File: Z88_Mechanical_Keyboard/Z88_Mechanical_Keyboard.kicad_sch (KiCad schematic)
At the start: 66 parts, among them SW1 SHIFT_RH, SW10 SHIFT_LH, SW11 SPACE, SW12 LEFT, SW13 RIGHT, SW14 DOWN, SW15 UP, SW16 ENTER, SW17 ESC, SW18 TAB, SW19 1, SW2 HELP, SW20 2, SW21 3, SW22 4, SW23 5, SW24 6, SW25 INDEX, SW26 DIAMOND, SW27 Q, SW28 W, SW29 E, SW3 [, SW30 R, SW31 T, SW32 Y, SW33 CAPS_LOCK, SW34 MENU, SW35 A, SW36 S, SW37 D, SW38 F, SW39 G, SW4 ], SW40 H, SW41 DOT, SW42 COMMA, SW43 Z, SW44 X, SW45 C, SW46 V, SW47 B, SW48 N, SW49 /, SW5 UNDERSCORE, SW50 SEMICOLON, SW51 L, SW52 M, SW53 K, SW54 J, SW55 U, SW56 7, SW57 £, SW58 DOUBLE_QUOTE, SW59 0, SW6 =, SW60 P, SW61 9, SW62 O, SW63 I, SW64 8, SW7 \, SW8 DELETE, SW9 SQUARE

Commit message: Progress commit
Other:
- company: (none) -> Brett Hallen
- title: (none) -> Z88 Mechanical Keyboard
- moved on the sheet: SK7
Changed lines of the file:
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@@
 	(generator_version "9.0")
 	(paper "A4")
+	(title_block
+		(title "Z88 Mechanical Keyboard")
+		(date "1-Jul-2025")
+		(rev "WIP")
+		(company "Brett Hallen")
+		(comment 1 "www.youtube.com/@Brfff")
+	)
 	(text_box "Columns      Rows\nCOL0 = A15   ROW0 = D7\nCOL1 = A14   ROW1 = D6\nCOL2 = A13   ROW2 = D5\nCOL3 = A12   ROW3 = D4\nCOL4 = A11   ROW4 = D3\nCOL5 = A10   ROW5 = D2\nCOL6 = A9    ROW6 = D1\nCOL7 = A8    ROW7 = D0"
 		(exclude_from_sim no)
@@
 	(global_label "ROW5"
 		(shape input)
-		(at 254 46.99 180)
+		(at 256.54 39.37 270)
 		(fields_autoplaced yes)
 		(effects
@@
 		)
 		(property "Intersheetrefs" "${INTERSHEET_REFS}"
-			(at 245.7534 46.99 0)
+			(at 256.54 47.6166 90)
 			(effects
 				(font
@@
 	(global_label "ROW2"
 		(shape input)
-		(at 254 29.21 180)
+		(at 238.76 39.37 270)
 		(fields_autoplaced yes)
 		(effects
@@
 		)
 		(property "Intersheetrefs" "${INTERSHEET_REFS}"
-			(at 245.7534 29.21 0)
+			(at 238.76 47.6166 90)
 			(effects
 				(font
@@
 	(global_label "ROW6"
 		(shape input)
-		(at 254 36.83 180)
+		(at 246.38 39.37 270)
 		(fields_autoplaced yes)
 		(effects
@@
 		)
 		(property "Intersheetrefs" "${INTERSHEET_REFS}"
-			(at 245.7534 36.83 0)
+			(at 246.38 47.6166 90)
 			(effects
 				(font
@@
 	(global_label "ROW4"
 		(shape input)
-		(at 254 34.29 180)
+		(at 243.84 39.37 270)
 		(fields_autoplaced yes)
 		(effects
@@
 		)
 		(property "Intersheetrefs" "${INTERSHEET_REFS}"
-			(at 245.7534 34.29 0)
+			(at 243.84 47.6166 90)
 			(effects
 				(font
@@
 	(global_label "ROW0"
 		(shape input)
-		(at 254 39.37 180)
+		(at 248.92 39.37 270)
 		(fields_autoplaced yes)
 		(effects
@@
 		)
 		(property "Intersheetrefs" "${INTERSHEET_REFS}"
-			(at 245.7534 39.37 0)
+			(at 248.92 47.6166 90)
 			(effects
 				(font
@@
 	(global_label "ROW7"
 		(shape input)
-		(at 254 41.91 180)
+		(at 251.46 39.37 270)
 		(fields_autoplaced yes)
 		(effects
@@
 		)
 		(property "Intersheetrefs" "${INTERSHEET_REFS}"
-			(at 245.7534 41.91 0)
+			(at 251.46 47.6166 90)
 			(effects
 				(font
@@
 	(global_label "ROW3"
 		(shape input)
-		(at 254 31.75 180)
+		(at 241.3 39.37 270)
 		(fields_autoplaced yes)
 		(effects
@@
 		)
 		(property "Intersheetrefs" "${INTERSHEET_REFS}"
-			(at 245.7534 31.75 0)
+			(at 241.3 47.6166 90)
 			(effects
 				(font
@@
 	(global_label "ROW1"
 		(shape input)
-		(at 254 44.45 180)
+		(at 254 39.37 270)
 		(fields_autoplaced yes)
 		(effects
@@
 		)
 		(property "Intersheetrefs" "${INTERSHEET_REFS}"
-			(at 245.7534 44.45 0)
+			(at 254 47.6166 90)
 			(effects
 				(font
@@
 	(symbol
 		(lib_id "Connector_Generic:Conn_01x08")
-		(at 259.08 36.83 0)
+		(at 246.38 34.29 90)
 		(unit 1)
 		(exclude_from_sim no)
@@
 		(on_board yes)
 		(dnp no)
-		(fields_autoplaced yes)
 		(property "Reference" "SK7"
-			(at 261.62 36.8299 0)
+			(at 248.92 27.94 90)
 			(effects
 				(font
@@
 		)
 		(property "Value" "Z80 Data Bus"
-			(at 261.62 39.3699 0)
+			(at 251.46 30.48 90)
 			(effects
 				(font
@@
 		)
 		(property "Footprint" "Connector_PinHeader_2.54mm:PinHeader_1x08_P2.54mm_Horizontal"
-			(at 259.08 36.83 0)
+			(at 246.38 34.29 0)
 			(effects
 				(font
@@
 		)
 		(property "Datasheet" "~"
-			(at 259.08 36.83 0)
+			(at 246.38 34.29 0)
 			(effects
 				(font
@@
 		)
 		(property "Description" "Generic connector, single row, 01x08, script generated (kicad-library-utils/schlib/autogen/connector/)"
-			(at 259.08 36.83 0)
+			(at 246.38 34.29 0)
 			(effects
 				(font

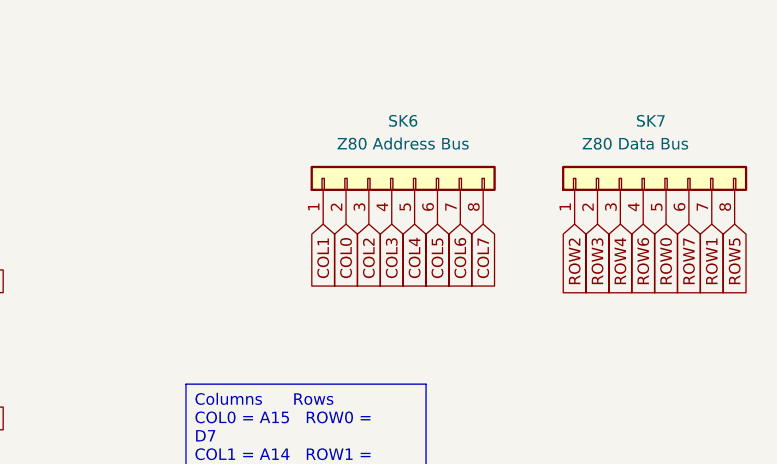
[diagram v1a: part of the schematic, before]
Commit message: Added 3D models
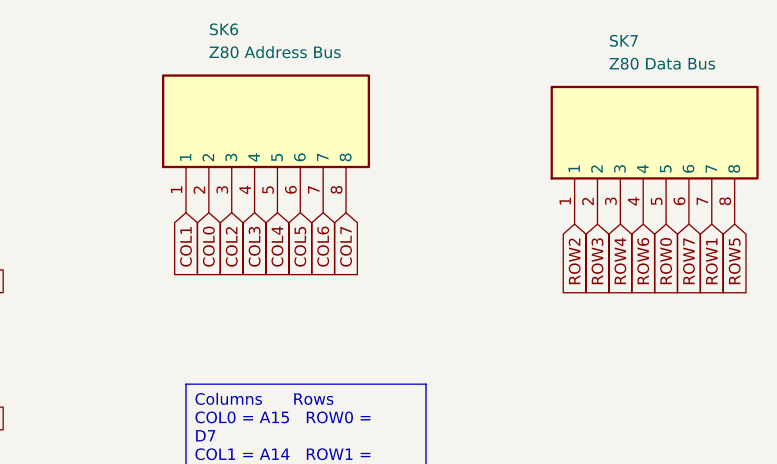
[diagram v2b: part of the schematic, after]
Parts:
- removed SK6: Z80 Address Bus, Connector_PinHeader_2.54mm:PinHeader_1x08_P2.54mm_Horizontal, symbol Connector_Generic:Conn_01x08
- removed SK7: Z80 Data Bus, Connector_PinHeader_2.54mm:PinHeader_1x08_P2.54mm_Horizontal, symbol Connector_Generic:Conn_01x08
- added SK6: Z80 Address Bus, Clueless_Engineer:55203148, symbol Clueless_Engineer:5-520314-8
- added SK7: Z80 Data Bus, Clueless_Engineer:55203148, symbol Clueless_Engineer:5-520314-8
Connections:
- net COL0: now also SK6.2
- net COL1: now also SK6.1
- net COL2: now also SK6.3
- net COL3: now also SK6.4
- net COL4: now also SK6.5
- net COL5: now also SK6.6
- net COL6: now also SK6.7
- net COL7: now also SK6.8
- net ROW0: now also SK7.5
- net ROW1: now also SK7.7
- net ROW2: now also SK7.1
- net ROW3: now also SK7.2
- net ROW4: now also SK7.3
- net ROW5: now also SK7.8
- net ROW6: now also SK7.4
- net ROW7: now also SK7.6

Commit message: Keyboard layout changes
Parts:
- added H1, H2: MountingHole, MountingHole:MountingHole_3.2mm_M3, symbol Mechanical:MountingHole
- SW19: value 1 -> ONE
- SW49: value / -> /FORWSLASH/
- SW57: value £ -> GBP
- SW59: value 0 -> ZERO
- SW6: value = -> EQUALS
- SW7: value \ -> \BACKSLASH\
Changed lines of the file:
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@@
 	)
 	(symbol
+		(lib_id "Mechanical:MountingHole")
+		(at 205.74 106.68 0)
+		(unit 1)
+		(exclude_from_sim yes)
+		(in_bom no)
+		(on_board yes)
+		(dnp no)
+		(fields_autoplaced yes)
+		(property "Reference" "H1"
+			(at 208.28 105.4099 0)
+			(effects
+				(font
+					(size 1.27 1.27)
+				)
+				(justify left)
+			)
+		)
+		(property "Value" "MountingHole"
+			(at 208.28 107.9499 0)
+			(effects
+				(font
+					(size 1.27 1.27)
+				)
+				(justify left)
+			)
+		)
+		(property "Footprint" "MountingHole:MountingHole_3.2mm_M3"
+			(at 205.74 106.68 0)
+			(effects
+				(font
+					(size 1.27 1.27)
+				)
+				(hide yes)
+			)
+		)
+		(property "Datasheet" "~"
+			(at 205.74 106.68 0)
+			(effects
+				(font
+					(size 1.27 1.27)
+				)
+				(hide yes)
+			)
+		)
+		(property "Description" "Mounting Hole without connection"
+			(at 205.74 106.68 0)
+			(effects
+				(font
+					(size 1.27 1.27)
+				)
+				(hide yes)
+			)
+		)
+		(instances
+			(project ""
+				(path "/52bc2244-0402-458b-a824-605619f8f036"
+					(reference "H1")
+					(unit 1)
+				)
+			)
+		)
+	)
+	(symbol
 		(lib_id "Switch:SW_Push_45deg")
 		(at 165.1 43.18 0)
@@
 			)
 		)
-		(property "Value" "1"
+		(property "Value" "ONE"
 			(at 82.55 69.85 0)
 			(effects
@@
 			)
 		)
-		(property "Value" "/"
+		(property "Value" "/FORWSLASH/"
 			(at 49.53 132.08 0)
 			(effects
@@
 			)
 		)
-		(property "Value" "="
+		(property "Value" "EQUALS"
 			(at 132.08 38.1 0)
 			(effects
@@
 			)
 		)
-		(property "Value" "\\"
+		(property "Value" "\\BACKSLASH\\"
 			(at 148.59 38.1 0)
 			(effects
@@
 			)
 		)
-		(property "Value" "0"
+		(property "Value" "ZERO"
 			(at 82.55 147.32 0)
 			(effects
@@
 	)
 	(symbol
+		(lib_id "Mechanical:MountingHole")
+		(at 205.74 114.3 0)
+		(unit 1)
+		(exclude_from_sim yes)
+		(in_bom no)
+		(on_board yes)
+		(dnp no)
+		(fields_autoplaced yes)
+		(property "Reference" "H2"
+			(at 208.28 113.0299 0)
+			(effects
+				(font
+					(size 1.27 1.27)
+				)
+				(justify left)
+			)
+		)
+		(property "Value" "MountingHole"
+			(at 208.28 115.5699 0)
+			(effects
+				(font
+					(size 1.27 1.27)
+				)
+				(justify left)
+			)
+		)
+		(property "Footprint" "MountingHole:MountingHole_3.2mm_M3"
+			(at 205.74 114.3 0)
+			(effects
+				(font
+					(size 1.27 1.27)
+				)
+				(hide yes)
+			)
+		)
+		(property "Datasheet" "~"
+			(at 205.74 114.3 0)
+			(effects
+				(font
+					(size 1.27 1.27)
+				)
+				(hide yes)
+			)
+		)
+		(property "Description" "Mounting Hole without connection"
+			(at 205.74 114.3 0)
+			(effects
+				(font
+					(size 1.27 1.27)
+				)
+				(hide yes)
+			)
+		)
+		(instances
+			(project "Z88_Mechanical_Keyboard"
+				(path "/52bc2244-0402-458b-a824-605619f8f036"
+					(reference "H2")
+					(unit 1)
+				)
+			)
+		)
+	)
+	(symbol
 		(lib_id "Switch:SW_Push_45deg")
 		(at 49.53 43.18 0)
@@
 			)
 		)
-		(property "Value" "£"
+		(property "Value" "GBP"
 			(at 49.53 147.32 0)
 			(effects

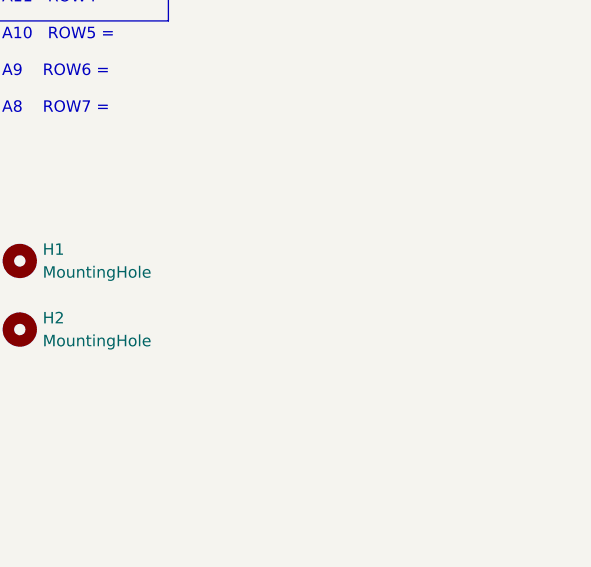
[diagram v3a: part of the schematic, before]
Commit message: Added T-cursor layout
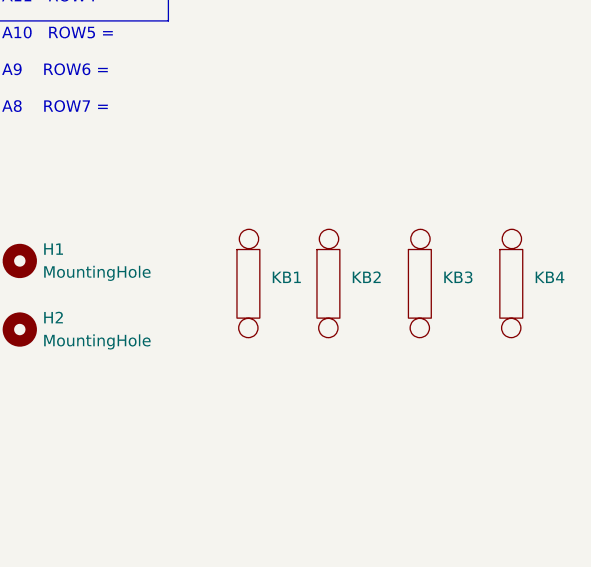
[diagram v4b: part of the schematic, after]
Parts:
- added KB1, KB2, KB3: ~, PCM_Mounting_Keyboard_Stabilizer:Stabilizer_Cherry_MX_2.00u, symbol Clueless_Engineer:Stabiliser
- added KB4: ~, PCM_Mounting_Keyboard_Stabilizer:Stabilizer_Cherry_MX_7.00u, symbol Clueless_Engineer:Stabiliser

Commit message: Routing completed
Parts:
- KB1: value ~ -> SHIFT_LH
- KB2: value ~ -> SHIFT_RH
- KB3: value ~ -> ENTER
- KB4: value ~ -> SPACE_BAR
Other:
- moved on the sheet: KB1, KB2, KB3, KB4
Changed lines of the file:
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@@
 	(title_block
 		(title "Z88 Mechanical Keyboard")
-		(date "1-Jul-2025")
-		(rev "WIP")
+		(date "4-Jul-2025")
+		(rev "A")
 		(company "Brett Hallen")
 		(comment 1 "www.youtube.com/@Brfff")
@@
 	(symbol
 		(lib_id "Clueless_Engineer:Stabiliser")
-		(at 232.41 107.95 0)
+		(at 207.01 127 0)
 		(unit 1)
 		(exclude_from_sim no)
@@
 		(fields_autoplaced yes)
 		(property "Reference" "KB1"
-			(at 233.68 108.5493 0)
+			(at 208.28 127.5993 0)
 			(effects
 				(font
@@
 			)
 		)
-		(property "Value" "~"
-			(at 233.68 110.4544 0)
+		(property "Value" "SHIFT_LH"
+			(at 208.28 129.5044 0)
 			(effects
 				(font
@@
 		)
 		(property "Footprint" "PCM_Mounting_Keyboard_Stabilizer:Stabilizer_Cherry_MX_2.00u"
-			(at 232.41 107.95 0)
+			(at 207.01 127 0)
 			(effects
 				(font
@@
 		)
 		(property "Datasheet" ""
-			(at 232.41 107.95 0)
+			(at 207.01 127 0)
 			(effects
 				(font
@@
 		)
 		(property "Description" ""
-			(at 232.41 107.95 0)
+			(at 207.01 127 0)
 			(effects
 				(font
@@
 	(symbol
 		(lib_id "Clueless_Engineer:Stabiliser")
-		(at 261.62 107.95 0)
+		(at 229.87 134.62 0)
 		(unit 1)
 		(exclude_from_sim no)
@@
 		(fields_autoplaced yes)
 		(property "Reference" "KB4"
-			(at 262.89 108.5493 0)
+			(at 231.14 135.2193 0)
 			(effects
 				(font
@@
 			)
 		)
-		(property "Value" "~"
-			(at 262.89 110.4544 0)
+		(property "Value" "SPACE_BAR"
+			(at 231.14 137.1244 0)
 			(effects
 				(font
@@
 		)
 		(property "Footprint" "PCM_Mounting_Keyboard_Stabilizer:Stabilizer_Cherry_MX_7.00u"
-			(at 261.62 107.95 0)
+			(at 229.87 134.62 0)
 			(effects
 				(font
@@
 		)
 		(property "Datasheet" ""
-			(at 261.62 107.95 0)
+			(at 229.87 134.62 0)
 			(effects
 				(font
@@
 		)
 		(property "Description" ""
-			(at 261.62 107.95 0)
+			(at 229.87 134.62 0)
 			(effects
 				(font
@@
 	(symbol
 		(lib_id "Clueless_Engineer:Stabiliser")
-		(at 241.3 107.95 0)
+		(at 255.27 127 0)
 		(unit 1)
 		(exclude_from_sim no)
@@
 		(fields_autoplaced yes)
 		(property "Reference" "KB2"
-			(at 242.57 108.5493 0)
+			(at 256.54 127.5993 0)
 			(effects
 				(font
@@
 			)
 		)
-		(property "Value" "~"
-			(at 242.57 110.4544 0)
+		(property "Value" "SHIFT_RH"
+			(at 256.54 129.5044 0)
 			(effects
 				(font
@@
 		)
 		(property "Footprint" "PCM_Mounting_Keyboard_Stabilizer:Stabilizer_Cherry_MX_2.00u"
-			(at 241.3 107.95 0)
+			(at 255.27 127 0)
 			(effects
 				(font
@@
 		)
 		(property "Datasheet" ""
-			(at 241.3 107.95 0)
+			(at 255.27 127 0)
 			(effects
 				(font
@@
 		)
 		(property "Description" ""
-			(at 241.3 107.95 0)
+			(at 255.27 127 0)
 			(effects
 				(font
@@
 	(symbol
 		(lib_id "Clueless_Engineer:Stabiliser")
-		(at 251.46 107.95 0)
+		(at 255.27 111.76 0)
 		(unit 1)
 		(exclude_from_sim no)
@@
 		(fields_autoplaced yes)
 		(property "Reference" "KB3"
-			(at 252.73 108.5493 0)
+			(at 256.54 112.3593 0)
 			(effects
 				(font
@@
 			)
 		)
-		(property "Value" "~"
-			(at 252.73 110.4544 0)
+		(property "Value" "ENTER"
+			(at 256.54 114.2644 0)
 			(effects
 				(font
@@
 		)
 		(property "Footprint" "PCM_Mounting_Keyboard_Stabilizer:Stabilizer_Cherry_MX_2.00u"
-			(at 251.46 107.95 0)
+			(at 255.27 111.76 0)
 			(effects
 				(font
@@
 		)
 		(property "Datasheet" ""
-			(at 251.46 107.95 0)
+			(at 255.27 111.76 0)
 			(effects
 				(font
@@
 		)
 		(property "Description" ""
-			(at 251.46 107.95 0)
+			(at 255.27 111.76 0)
 			(effects
 				(font

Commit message: Final tweaks before test fabrication
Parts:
- SW12: value LEFT -> VASEN
- SW13: value RIGHT -> OIKEIN
- SW14: value DOWN -> ALAS
- SW15: value UP -> YLÖS
- SW19: value ONE -> YKSI
- SW2: value HELP -> APUA!
- SW20: value 2 -> KAKSI
- SW21: value 3 -> KOLME
- SW22: value 4 -> NELJÄ
- SW23: value 5 -> VIISI
- SW24: value 6 -> KUUSI
- SW56: value 7 -> SEITSEMÄN
- SW59: value ZERO -> NOLLA
- SW61: value 9 -> YHDEKSÄN
- SW64: value 8 -> KAHDEKSAN
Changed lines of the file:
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@@
 		(comment 1 "www.youtube.com/@Brfff")
 	)
+	(text_box "SUOMI       ENGLISH\nNOLLA     = ZERO\nYKSI      = ONE\nKAKSI     = TWO\nKOLME     = THREE\nNELJÄ     = FOUR\nVIISI     = FIVE\nKUUSI     = SIX\nSEITSEMÄN = SEVEN\nKAHDEKSAN = EIGHT\nYHDEKSÄN  = NINE\n\nVASEN     = LEFT\nOIKEIN    = RIGHT\nYLÖS      = UP\nALAS      = DOWN\nAPUA!     = HELP!"
+		(exclude_from_sim no)
+		(at 226.06 57.15 0)
+		(size 25.4 39.37)
+		(margins 0.9525 0.9525 0.9525 0.9525)
+		(stroke
+			(width 0)
+			(type solid)
+		)
+		(fill
+			(type none)
+		)
+		(effects
+			(font
+				(face "Consolas")
+				(size 1.27 1.27)
+			)
+			(justify left top)
+		)
+	)
 	(text_box "Columns      Rows\nCOL0 = A15   ROW0 = D7\nCOL1 = A14   ROW1 = D6\nCOL2 = A13   ROW2 = D5\nCOL3 = A12   ROW3 = D4\nCOL4 = A11   ROW4 = D3\nCOL5 = A10   ROW5 = D2\nCOL6 = A9    ROW6 = D1\nCOL7 = A8    ROW7 = D0"
 		(exclude_from_sim no)
@@
 			)
 		)
-		(property "Value" "9"
+		(property "Value" "YHDEKSÄN"
 			(at 115.57 147.32 0)
 			(effects
@@
 			)
 		)
-		(property "Value" "ONE"
+		(property "Value" "YKSI"
 			(at 82.55 69.85 0)
 			(effects
@@
 			)
 		)
-		(property "Value" "DOWN"
+		(property "Value" "ALAS"
 			(at 132.08 53.34 0)
 			(effects
@@
 			)
 		)
-		(property "Value" "4"
+		(property "Value" "NELJÄ"
 			(at 132.08 69.85 0)
 			(effects
@@
 			)
 		)
-		(property "Value" "RIGHT"
+		(property "Value" "OIKEIN"
 			(at 115.57 53.34 0)
 			(effects
@@
 			)
 		)
-		(property "Value" "3"
+		(property "Value" "KOLME"
 			(at 115.57 69.85 0)
 			(effects
@@
 			)
 		)
-		(property "Value" "8"
+		(property "Value" "KAHDEKSAN"
 			(at 165.1 147.32 0)
 			(effects
@@
 			)
 		)
-		(property "Value" "6"
+		(property "Value" "KUUSI"
 			(at 165.1 69.85 0)
 			(effects
@@
 			)
 		)
-		(property "Value" "5"
+		(property "Value" "VIISI"
 			(at 148.59 69.85 0)
 			(effects
@@
 			)
 		)
-		(property "Value" "7"
+		(property "Value" "SEITSEMÄN"
 			(at 165.1 132.08 0)
 			(effects
@@
 			)
 		)
-		(property "Value" "LEFT"
+		(property "Value" "VASEN"
 			(at 99.06 53.34 0)
 			(effects
@@
 			)
 		)
-		(property "Value" "ZERO"
+		(property "Value" "NOLLA"
 			(at 82.55 147.32 0)
 			(effects
@@
 			)
 		)
-		(property "Value" "HELP"
+		(property "Value" "APUA!"
 			(at 66.04 38.1 0)
 			(effects
@@
 			)
 		)
-		(property "Value" "2"
+		(property "Value" "KAKSI"
 			(at 99.06 69.85 0)
 			(effects
@@
 			)
 		)
-		(property "Value" "UP"
+		(property "Value" "YLÖS"
 			(at 148.59 53.34 0)
 			(effects
